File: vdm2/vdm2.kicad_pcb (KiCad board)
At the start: 2 copper layers, 254 x 138.2 mm, 160 parts, among them IC1 7406, IC10 74LS109, IC11 74LS138, IC12 74LS86, IC13 74LS109, IC14 74LS02, IC15 74LS00, IC16 74LS109, IC17 74LS175, IC18 74LS132, IC19 74LS04, IC2 74LS163, IC20 74LS163, IC21 74LS163, IC22 74LS163, IC23 74LS157, IC24 74LS157, IC25 4049, IC26 4029, IC27 4029, IC28 74LS157, IC29 DM8131, IC3 74166, IC30 4001, IC31 4042, IC32 4042, IC33 74LS08, IC34 74LS08, IC35 74LS00, IC36 74LS04, IC37 8836, IC38 74LS367, IC39 74LS367, IC4 MCM6575, IC40 74LS10, IC41 2102, IC42 2102, IC43 2102, IC44 2102, IC45 2102, IC46 2102, IC47 2102, IC48 2102, IC49 L7805, IC5 74LS175, IC6 74LS175, IC7 74LS20, IC8 93L16, IC9 74LS10, J2 Jumper_3_Open, J4 Jumper_2_Open, J5 Jumper_2_Open, Q1 2N2907, SW1 SW_DIP_x06, U1 L7812, Y1 Crystal

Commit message: Placement close to done
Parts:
- moved C24 433.3 mm to (370.5, 176.5), turned to 0 degrees
- moved C17 430.7 mm to (385.2, 198.3), turned to 0 degrees
- moved C12 428.9 mm to (378.1, 132.3), turned to 0 degrees
- moved C11 428.4 mm to (387.8, 194.2), turned to 0 degrees
- moved C35 426.9 mm to (374.9, 156.6), turned to 0 degrees
- moved C14 421.0 mm to (366.8, 162.4), turned to 0 degrees
- moved C26 402.9 mm to (387.8, 186.2), turned to 0 degrees
- moved C37 394.5 mm to (378.6, 176.6), turned to 0 degrees
- moved C45 382.7 mm to (405.8, 175.5)
- moved C33 381.3 mm to (358.6, 158.4), turned to 0 degrees
- moved C43 368.1 mm to (383.7, 164.4)
- moved C46 368.0 mm to (397.6, 179.6)
- moved C48 366.9 mm to (372.9, 172.4)
- moved C41 361.6 mm to (383.7, 160.4)
- moved C32 361.1 mm to (359.2, 142.7), turned to 0 degrees
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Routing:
- net GND: track 917.5 -> 226.7 mm, vias 10 -> 0
- net +5V: track 628.9 -> 46.1 mm, vias 9 -> 0
- net Net-(IC28-Pad4): track 258.9 -> 0.00 mm
- net Net-(C8-Pad1): track 0.00 -> 239.5 mm, vias 0 -> 1
- net Net-(IC24-Pad7): track 177.5 -> 0.00 mm
- net Net-(IC23-Pad12): track 168.5 -> 0.00 mm, vias 3 -> 0
- net Net-(IC23-Pad9): track 155.2 -> 0.00 mm, vias 2 -> 0
- net Net-(IC23-Pad7): track 147.4 -> 0.00 mm, vias 2 -> 0
- net Net-(IC23-Pad4): track 139.4 -> 0.00 mm
- net Net-(C39-Pad1): track 306.9 -> 179.4 mm, vias 1 -> 5
- net Net-(IC32-Pad7): track 124.7 -> 0.00 mm, vias 4 -> 0
- net Net-(IC32-Pad13): track 120.8 -> 0.00 mm, vias 7 -> 0
- net Net-(IC28-Pad7): track 114.9 -> 0.00 mm
- net Net-(IC28-Pad9): track 114.5 -> 0.00 mm
- net Net-(IC18-Pad11): track 113.1 -> 0.00 mm
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- removed copper zone on F.Cu, net GND

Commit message: Progress
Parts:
- added C49: .1uf, Capacitor_THT:C_Disc_D6.0mm_W2.5mm_P5.00mm, F.Cu at (194.9, 24.1)
- added C50: .1uf, Capacitor_THT:C_Disc_D6.0mm_W2.5mm_P5.00mm, F.Cu at (209.8, 24.1)
- added C51: .1uf, Capacitor_THT:C_Disc_D6.0mm_W2.5mm_P5.00mm, F.Cu at (64.1, 59.7)
- added C52: .1uf, Capacitor_THT:C_Disc_D6.0mm_W2.5mm_P5.00mm, F.Cu at (224.8, 24.1)
- added C53: .1uf, Capacitor_THT:C_Disc_D6.0mm_W2.5mm_P5.00mm, F.Cu at (79.5, 59.7)
- added C54: .1uf, Capacitor_THT:C_Disc_D6.0mm_W2.5mm_P5.00mm, F.Cu at (240.0, 24.1)
- added C55: .1uf, Capacitor_THT:C_Disc_D6.0mm_W2.5mm_P5.00mm, F.Cu at (140.5, 59.6)
- added C56: .1uf, Capacitor_THT:C_Disc_D6.0mm_W2.5mm_P5.00mm, F.Cu at (48.9, 58.4)
- added C57: .1uf, Capacitor_THT:C_Disc_D6.0mm_W2.5mm_P5.00mm, F.Cu at (94.7, 59.6)
- added C58: .1uf, Capacitor_THT:C_Disc_D6.0mm_W2.5mm_P5.00mm, F.Cu at (182.4, 59.6)
- added C59: .1uf, Capacitor_THT:C_Disc_D6.0mm_W2.5mm_P5.00mm, F.Cu at (110.2, 59.6)
- added C60: .1uf, Capacitor_THT:C_Disc_D6.0mm_W2.5mm_P5.00mm, F.Cu at (254.5, 24.1)
- added C61: .1uf, Capacitor_THT:C_Disc_D6.0mm_W2.5mm_P5.00mm, F.Cu at (125.2, 59.6)
- added C62: .1uf, Capacitor_THT:C_Disc_D6.0mm_W2.5mm_P5.00mm, F.Cu at (212.7, 59.7)
- added C63: .1uf, Capacitor_THT:C_Disc_D6.0mm_W2.5mm_P5.00mm, F.Cu at (139.3, -6.67)
- added C64: .1uf, Capacitor_THT:C_Disc_D6.0mm_W2.5mm_P5.00mm, F.Cu at (241.9, 59.7)
- added C65: .1uf, Capacitor_THT:C_Disc_D6.0mm_W2.5mm_P5.00mm, F.Cu at (155.7, 59.7)
- added C66: .1uf, Capacitor_THT:C_Disc_D6.0mm_W2.5mm_P5.00mm, F.Cu at (143.4, -6.67)
- added C67: .1uf, Capacitor_THT:C_Disc_D6.0mm_W2.5mm_P5.00mm, F.Cu at (147.4, -6.67)
- added C68: .1uf, Capacitor_THT:C_Disc_D6.0mm_W2.5mm_P5.00mm, F.Cu at (151.5, -6.67)
- IC49: footprint Package_TO_SOT_THT:TO-220-3_Horizontal_TabUp -> Package_TO_SOT_THT:TO-220-3_Horizontal_TabDown
- moved C2 361.3 mm to (41.7, 116.8), turned to 90 degrees
- moved C17 361.3 mm to (41.3, 87.6), turned to 90 degrees
- moved C5 327.7 mm to (77.0, 116.8), turned to 90 degrees
- moved C3 319.5 mm to (59.2, 116.8), turned to 90 degrees
- moved C18 315.8 mm to (56.5, 87.6), turned to 90 degrees
- moved C23 302.0 mm to (71.8, 87.6), turned to 90 degrees
- moved C26 299.7 mm to (104.8, 87.6), turned to 90 degrees
- moved C32 299.2 mm to (84.5, 24.1), turned to 90 degrees
- moved C24 294.7 mm to (89.5, 87.6), turned to 90 degrees
- moved C35 291.8 mm to (114.9, 24.1), turned to 90 degrees
- moved C33 291.1 mm to (100.3, 24.1), turned to 90 degrees
- moved C43 271.4 mm to (120.3, 99.3), turned to 270 degrees
- moved C44 268.4 mm to (135.4, 99.1), turned to 270 degrees
- moved C37 261.9 mm to (165.7, 24.1), turned to 90 degrees
- moved C11 261.4 mm to (138.2, 116.6), turned to 90 degrees
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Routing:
- net GND: track 226.7 -> 2090.8 mm, vias 0 -> 45
- net +5V: track 46.1 -> 1610.7 mm, vias 0 -> 21
- net Net-(IC1-Pad1): track 0.00 -> 289.4 mm, vias 0 -> 2
- net Net-(IC32-Pad7): track 0.00 -> 277.0 mm, vias 0 -> 4
- net Net-(ADDR1-Pad13): track 0.00 -> 245.2 mm, vias 0 -> 4
- net Net-(IC39-Pad10): track 0.00 -> 243.2 mm, vias 0 -> 4
- net Net-(IC1-Pad4): track 0.00 -> 243.1 mm, vias 0 -> 3
- net Net-(IC26-Pad15): track 0.00 -> 240.9 mm
- net Net-(IC13-Pad6): track 0.00 -> 237.5 mm, vias 0 -> 3
- net Net-(IC24-Pad7): track 0.00 -> 233.0 mm, vias 0 -> 2
- net Net-(IC23-Pad9): track 0.00 -> 226.4 mm, vias 0 -> 1
- net Net-(IC30-Pad13): track 0.00 -> 221.9 mm, vias 0 -> 2
- net Net-(IC24-Pad9): track 0.00 -> 213.9 mm, vias 0 -> 1
- net Net-(IC23-Pad7): track 0.00 -> 212.8 mm, vias 0 -> 2
- net Net-(IC16-Pad14): track 0.00 -> 210.2 mm, vias 0 -> 2
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- added copper zone on B.Cu, net +5V
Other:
- net class Default: clearance 0.2 -> 0.254
- rule trace_clearance: 0.2 -> 0.254

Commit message: Very close to fully routed
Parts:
- removed C63, C66, C67, C68: .1uf, Capacitor_THT:C_Disc_D6.0mm_W2.5mm_P5.00mm
- moved D1 64.4 mm to (52.1, 51.2)
- moved R6 64.4 mm to (52.1, 48.3)
- moved C8 59.8 mm to (71.8, 45.7), turned to 90 degrees
- moved C7 55.5 mm to (91.9, 46.1)
- moved U1 55.1 mm to (81.4, 46.0)
- moved C9 49.8 mm to (104.6, 46.1)
- moved R14 47.5 mm to (228.0, 56.5), turned to 270 degrees
- moved R21 47.4 mm to (250.8, 73.7), turned to 180 degrees
- moved IC1 28.4 mm to (231.1, 58.4)
- moved IC40 28.4 mm to (236.2, 86.4)
- moved R11 22.4 mm to (267.3, 39.6), turned to 180 degrees
- moved C20 15.6 mm to (198.2, 63.1), turned to 270 degrees
- moved R40 13.5 mm to (224.8, 61.7)
- moved R37 2.92 mm to (217.2, 64.9)
- moved R38 2.92 mm to (217.2, 71.5)
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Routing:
- net Net-(IC15-Pad13): track 0.00 -> 256.0 mm, vias 0 -> 3
- net +5V: track 1610.7 -> 1855.7 mm, vias 21 -> 39
- net Net-(IC19-Pad2): track 0.00 -> 230.5 mm, vias 0 -> 3
- net Net-(IC10-Pad12): track 28.9 -> 258.9 mm, vias 0 -> 3
- net Net-(IC13-Pad4): track 138.1 -> 339.1 mm, vias 2 -> 7
- net Net-(C30-Pad2): track 89.6 -> 286.8 mm, vias 1 -> 2
- net Net-(IC14-Pad10): track 0.00 -> 194.7 mm, vias 0 -> 1
- net Net-(IC14-Pad11): track 0.00 -> 185.6 mm, vias 0 -> 2
- net Net-(IC11-Pad6): track 0.00 -> 185.3 mm, vias 0 -> 2
- net Net-(C28-Pad1): track 108.3 -> 280.4 mm, vias 1 -> 4
- net Net-(IC17-Pad11): track 0.00 -> 159.0 mm, vias 0 -> 2
- net Net-(IC1-Pad9): track 0.00 -> 151.5 mm, vias 0 -> 4
- net Net-(IC13-Pad13): track 141.0 -> 285.1 mm, vias 3 -> 6
- net Net-(IC20-Pad1): track 0.00 -> 144.0 mm, vias 0 -> 3
- net Net-(IC10-Pad13): track 0.00 -> 143.2 mm, vias 0 -> 2
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
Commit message: Fully routed
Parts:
- moved R21 1.40 mm to (250.8, 72.3)
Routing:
- net Net-(IC17-Pad14): track 0.00 -> 117.7 mm, vias 0 -> 2
- net GND: track 2137.1 -> 2248.5 mm
- net Net-(IC11-Pad3): track 45.6 -> 114.2 mm, vias 0 -> 1
- net Net-(IC2-Pad14): track 39.9 -> 93.5 mm, vias 1 -> 3
- net Net-(IC15-Pad13): track 256.0 -> 229.2 mm, vias 3 -> 2
- net Net-(IC13-Pad15): track 138.6 -> 128.6 mm
- net Net-(C28-Pad1): track 280.4 -> 271.4 mm, vias 4 -> 3
- net Net-(IC36-Pad8): track 127.3 -> 120.5 mm
- net Net-(IC39-Pad2): track 210.0 -> 216.7 mm
- net Net-(IC11-Pad4): track 122.6 -> 116.2 mm
- net Net-(IC13-Pad4): track 339.1 -> 334.8 mm, vias 7 -> 6
- net Net-(C34-Pad2): track 151.6 -> 155.3 mm, vias 3 -> 1
- net Net-(C29-Pad1): track 112.3 -> 116.0 mm
- net Net-(IC1-Pad2): track 196.7 -> 193.2 mm, vias 5 -> 4
- net Net-(IC10-Pad12): track 258.9 -> 255.7 mm
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
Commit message: really getting close
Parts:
- removed U1: L7812, Package_TO_SOT_THT:TO-220-3_Vertical
- added IC50: L7812, Package_TO_SOT_THT:TO-92_Inline, F.Cu at (87.8, 48.5)
- moved R40 195.6 mm to (29.2, 64.8), turned to 0 degrees
- moved C3 190.8 mm to (227.3, 26.7)
- moved R42 169.6 mm to (29.2, 79.8), turned to 0 degrees
- moved R25 149.5 mm to (68.6, 74.7), turned to 90 degrees
- moved C58 132.5 mm to (62.9, 116.8)
- moved R23 109.2 mm to (263.5, 106.7), turned to 90 degrees
- moved C34 107.6 mm to (215.5, 47.0), turned to 270 degrees
- moved R24 107.3 mm to (207.0, 44.5), turned to 270 degrees
- moved D3 106.5 mm to (259.7, 106.7), turned to 90 degrees
- moved D2 103.9 mm to (255.9, 106.7), turned to 90 degrees
- moved R22 101.6 mm to (252.1, 106.7), turned to 90 degrees
- moved Q1 99.7 mm to (221.9, 48.3), turned to 270 degrees
- moved C60 88.0 mm to (174.1, 59.9)
- moved R11 81.9 mm to (185.4, 38.1), turned to 90 degrees
- moved C25 75.9 mm to (255.9, 90.2)
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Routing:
- net GND: track 2248.5 -> 1403.4 mm, vias 49 -> 1
- net +5V: track 1852.7 -> 1337.4 mm, vias 38 -> 25
- net Net-(C8-Pad1): track 194.9 -> 11.4 mm, vias 1 -> 0
- net Net-(IC12-Pad2): track 122.8 -> 0.00 mm, vias 2 -> 0
- net Net-(IC1-Pad9): track 152.1 -> 29.4 mm, vias 4 -> 0
- net Net-(C34-Pad2): track 155.3 -> 32.9 mm, vias 1 -> 0
- net Net-(IC13-Pad4): track 334.8 -> 225.1 mm, vias 6 -> 5
- net Net-(C34-Pad1): track 134.1 -> 34.0 mm, vias 2 -> 1
- net Net-(IC2-Pad1): track 128.1 -> 35.7 mm, vias 3 -> 0
- net Net-(C29-Pad2): track 140.5 -> 54.6 mm
- net Net-(IC13-Pad5): track 173.7 -> 89.8 mm, vias 2 -> 0
- net Net-(C31-Pad2): track 124.5 -> 42.7 mm, vias 2 -> 0
- net Net-(C29-Pad1): track 116.0 -> 41.2 mm
- net Net-(IC17-Pad11): track 159.6 -> 85.6 mm, vias 2 -> 1
- net Net-(IC16-Pad14): track 137.1 -> 63.6 mm, vias 2 -> 0
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- added copper zone on F.Cu, net +5V
- added copper zone on B.Cu, net GND
- added copper zone on F.Cu, net GND
- removed copper zone on B.Cu, net +5V
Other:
- board text added: "REPRODUCTION OF VDM-1 (MADE IN 2021)"
- board text added: "VDM-2021"
- board text added: "github.com/physicsrob/vdm2021"

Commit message: Done
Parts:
- IC50: footprint Package_TO_SOT_THT:TO-92_Inline -> Package_TO_SOT_THT:TO-92_Inline_Wide
- moved J2 6.48 mm to (233.8, 139.7)
- moved C57 0.58 mm to (99.1, 59.9)
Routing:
- net GND: track 1403.4 -> 2765.9 mm, vias 1 -> 42
- net +5V: track 1337.4 -> 1739.9 mm, vias 25 -> 24
- net Net-(C8-Pad1): track 11.4 -> 133.8 mm
- net Net-(IC39-Pad13): track 68.2 -> 140.1 mm
- net Net-(IC1-Pad2): track 152.6 -> 144.0 mm
- net Net-(IC38-Pad6): track 142.1 -> 149.7 mm
- net Net-(IC24-Pad7): track 229.9 -> 237.5 mm
- net Net-(IC10-Pad3): track 81.7 -> 74.1 mm
- net Net-(IC32-Pad7): track 288.4 -> 295.8 mm
- net Net-(IC33-Pad5): track 68.0 -> 61.6 mm
- net Net-(IC12-Pad2): track 0.00 -> 6.35 mm
- net Net-(J2-Pad1): track 110.4 -> 116.1 mm
- net Net-(IC1-Pad4): track 221.4 -> 217.2 mm
- net Net-(J4-Pad1): track 62.5 -> 58.4 mm
- net Net-(IC29-Pad11): track 74.5 -> 78.6 mm
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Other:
- board text added: "github.com/physicsrob/vdm1"
- board text removed: "github.com/physicsrob/vdm2021"

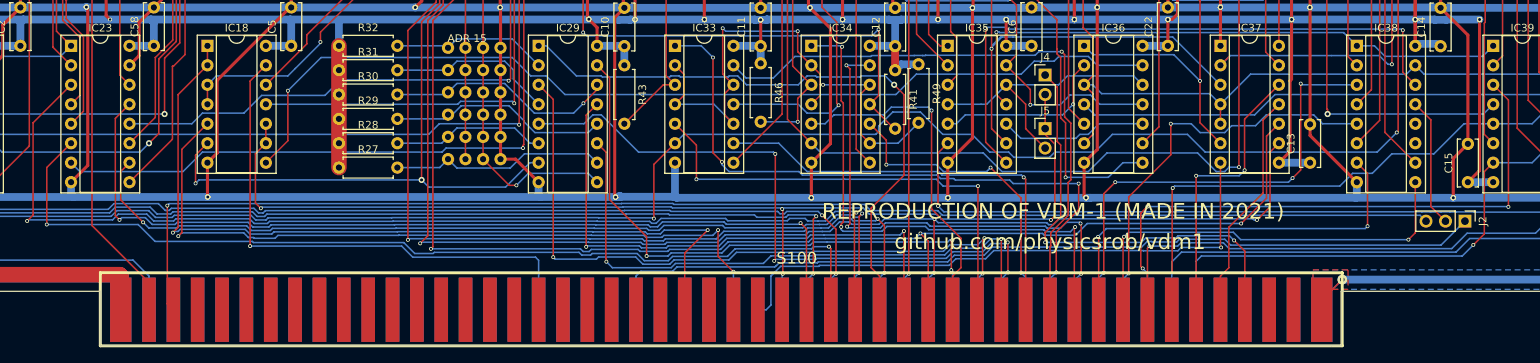
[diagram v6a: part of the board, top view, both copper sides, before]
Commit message: Fixed s100 connector alignment
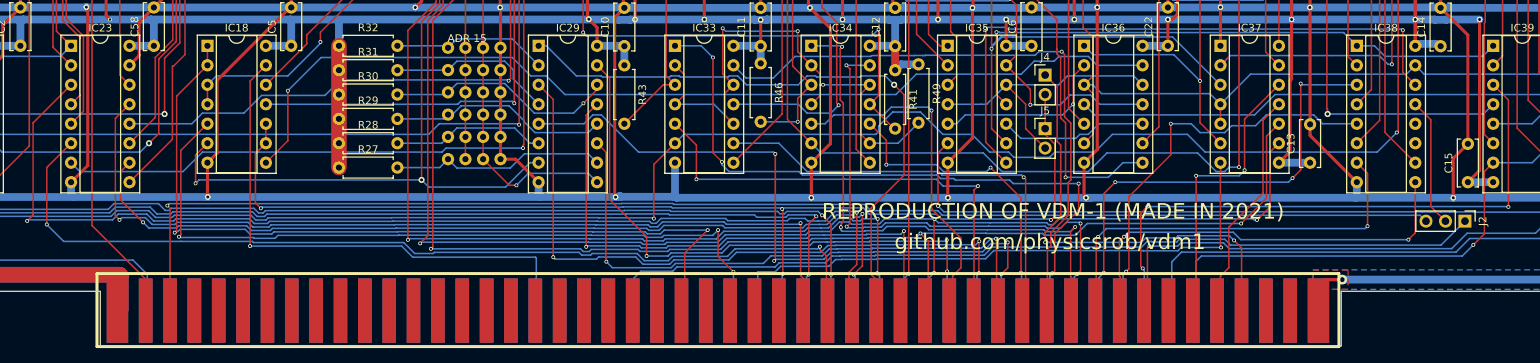
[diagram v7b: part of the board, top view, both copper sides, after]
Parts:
- moved S100 0.44 mm to (55.4, 156.1)
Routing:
- net Net-(IC39-Pad13): track 140.1 -> 83.7 mm, vias 2 -> 1
- net GND: track 2765.9 -> 2769.1 mm
- net Net-(IC29-Pad5): track 88.1 -> 89.6 mm
- net Net-(IC29-Pad3): track 91.3 -> 89.7 mm
- net Net-(IC37-Pad7): track 77.1 -> 77.8 mm
- net Net-(IC23-Pad6): track 125.2 -> 124.5 mm
- net Net-(IC23-Pad3): track 143.7 -> 144.3 mm
- net Net-(IC34-Pad1): track 70.4 -> 71.0 mm
- net Net-(IC29-Pad15): track 77.5 -> 76.9 mm
- net Net-(IC24-Pad6): track 139.3 -> 138.8 mm

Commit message: Small redesign for better thermal performance
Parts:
- added HEAT: Heat Sink, vdm2:heatsink, F.Cu at (50.2, 36.9)
- C4: value .1uf -> 1uf; footprint Capacitor_THT:C_Disc_D6.0mm_W2.5mm_P5.00mm -> Capacitor_THT:CP_Radial_Tantal_D6.0mm_P2.50mm
- IC49: footprint Package_TO_SOT_THT:TO-220-3_Horizontal_TabDown -> vdm2:TO-220-3_Horizontal_TabDown
- VIDEO1: footprint Connector_Coaxial:BNC_TEConnectivity_1478204_Vertical -> vdm2:bnc-5-16345033
- Y1: footprint Crystal:Crystal_HC49-U_Horizontal_1EP_style2 -> Crystal:Crystal_HC50_Horizontal
- moved R45 236.0 mm to (254.0, 140.3)
- moved R48 235.4 mm to (254.0, 143.5)
- moved IC31 221.8 mm to (255.9, 116.8)
- moved C56 208.4 mm to (252.7, 116.8)
- moved C51 202.8 mm to (263.5, 113.7), turned to 180 degrees
- moved IC26 193.8 mm to (241.9, 116.8)
- moved C9 70.5 mm to (45.7, 78.1), turned to 180 degrees
- moved IC50 52.3 mm to (40.6, 71.1)
- moved C7 52.0 mm to (50.1, 71.1)
- moved C8 46.7 mm to (36.2, 71.1), turned to 180 degrees
- moved R40 43.2 mm to (29.8, 108.0)
- moved R6 39.6 mm to (32.4, 78.1)
- moved R42 32.0 mm to (29.8, 111.8)
- moved R25 28.0 mm to (61.0, 101.6)
- moved D1 27.0 mm to (57.1, 78.1), turned to 180 degrees
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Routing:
- net Net-(IC13-Pad3): track 43.0 -> 244.8 mm, vias 1 -> 2
- net +12V: track 80.2 -> 155.6 mm
- net Net-(R6-Pad1): track 171.2 -> 114.0 mm
- net GND: track 2769.1 -> 2716.8 mm, vias 42 -> 150
- net Net-(C9-Pad2): track 115.8 -> 167.7 mm
- net Net-(C30-Pad2): track 213.3 -> 169.2 mm, vias 1 -> 0
- net Net-(C8-Pad1): track 133.8 -> 104.7 mm
- net Net-(IC35-Pad8): track 81.1 -> 56.5 mm, vias 2 -> 1
- net Net-(C19-Pad2): track 66.0 -> 89.0 mm, vias 2 -> 0
- net Net-(IC31-Pad13): track 202.8 -> 180.9 mm, vias 3 -> 2
- net Net-(IC31-Pad14): track 183.1 -> 204.5 mm
- net Net-(IC31-Pad7): track 192.9 -> 172.3 mm, vias 2 -> 1
- net Net-(IC19-Pad5): track 18.1 -> 36.7 mm
- net Net-(IC26-Pad13): track 25.0 -> 8.45 mm
- net Net-(C19-Pad1): track 2.98 -> 19.2 mm
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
